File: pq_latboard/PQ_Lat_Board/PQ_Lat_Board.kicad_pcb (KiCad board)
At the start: 6 copper layers, 48 x 48 mm, 12 parts, among them IC1 TCN75AVUA713-VAO, J1 Conn_01x11_MountingPin

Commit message: designs updated
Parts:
- added REF**: MountingHole_2.2mm_M2_Pad, MountingHole:MountingHole_2.2mm_M2_Pad, F.Cu at (81.0, 46.0)
- added REF**: MountingHole_2.2mm_M2_Pad, MountingHole:MountingHole_2.2mm_M2_Pad, F.Cu at (121.0, 87.0)
- added REF**: MountingHole_2.2mm_M2_Pad, MountingHole:MountingHole_2.2mm_M2_Pad, F.Cu at (79.0, 84.0)
- added REF**: MountingHole_2.2mm_M2_Pad, MountingHole:MountingHole_2.2mm_M2_Pad, F.Cu at (119.0, 46.0)
- moved GA0 1.96 mm to (107.2, 55.6)
- moved GA1 1.96 mm to (109.6, 55.6)
- moved GA2 1.96 mm to (112.0, 55.6)
- moved IC1 1.96 mm to (103.6, 53.4)
- moved VA1 1.96 mm to (109.7, 50.3)
- moved VA2 1.96 mm to (112.0, 50.3)
- moved J1 1.96 mm to (107.7, 63.1)
- moved VA0 1.96 mm to (107.3, 50.3)
- moved JP1 1.96 mm to (82.8, 66.0)
- moved D7 1.96 mm to (99.0, 46.1)
- moved R1 1.96 mm to (98.1, 52.9)
- moved R2 1.96 mm to (100.5, 52.9)
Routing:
- net /GND: track 53.6 -> 41.4 mm, vias 68 -> 42

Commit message: lots of changes
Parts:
- removed D7: D_Photo, NSL_misc:SLCD-61N8
- removed R1, R2: 5k, easyeda:R0805
- added ?: , , F.Cu at (78.0, 66.0)
- added C1: 100 nF, Capacitor_SMD:C_0603_1608Metric, F.Cu at (100.1, 51.5)
- added D1: D_Photo, GGS_Miscellaneous:SLCD-61N8, B.Cu at (99.0, 45.5)
- GA0, GA1, GA2, VA0, VA1, VA2: value 5k -> 0R; footprint easyeda:R0805 -> Resistor_SMD:R_0805_2012Metric
- H1, H2, H3, H4: renamed from REF**; value MountingHole_2.2mm_M2_Pad -> MountingHole_Pad
- IC1: footprint easyeda:SOP65P490X110-8N -> Package_SO:SOP-8_3.9x4.9mm_P1.27mm
- moved GA0 0.20 mm to (107.4, 55.6)
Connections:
- net /GND renamed GND
- net /Pout renamed /SOLAR
- J1 pad 2: /ADCS_GND -> /ADCS
- J1 pad 3: /ADCS -> /VCC_MAG
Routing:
- net GND: track 41.4 -> 23.1 mm, vias 42 -> 34
- net /SDA: track 13.6 -> 8.59 mm
- net Net-(GA1-Pad2): track 17.0 -> 21.6 mm
- net /VCC: track 32.9 -> 29.1 mm
- net /SCL: track 12.2 -> 8.56 mm
- net /Antenna Connector: track 0.91 -> 3.73 mm
- net Net-(GA2-Pad2): track 12.6 -> 11.5 mm
- net (no net): vias 1 -> 0
- added copper zone on F.Cu, net /Antenna Connector
- added copper zone on B.Cu, net /SOLAR

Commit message: files changed
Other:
- board text added: "Extend temp sensor footprint fopr dual compatibility Hole positioning Solar Cells pads"
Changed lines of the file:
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@@
   (gr_line (start 120 62) (end 120 70) (layer "Edge.Cuts") (width 0.15))
   (gr_line (start 120 70) (end 123 70) (layer "Edge.Cuts") (width 0.15))
+  (gr_text "Extend temp sensor footprint fopr dual compatibility\nHole positioning\nSolar Cells pads" (at 93 111.4) (layer "F.Cu")
+    (effects (font (size 1.5 1.5) (thickness 0.3)) (justify left))
+  )
   (gr_text "LATERAL BOARD" (at 89.2 86.525) (layer "F.SilkS")
     (effects (font (size 2.032 2.032) (thickness 0.203)) (justify left))

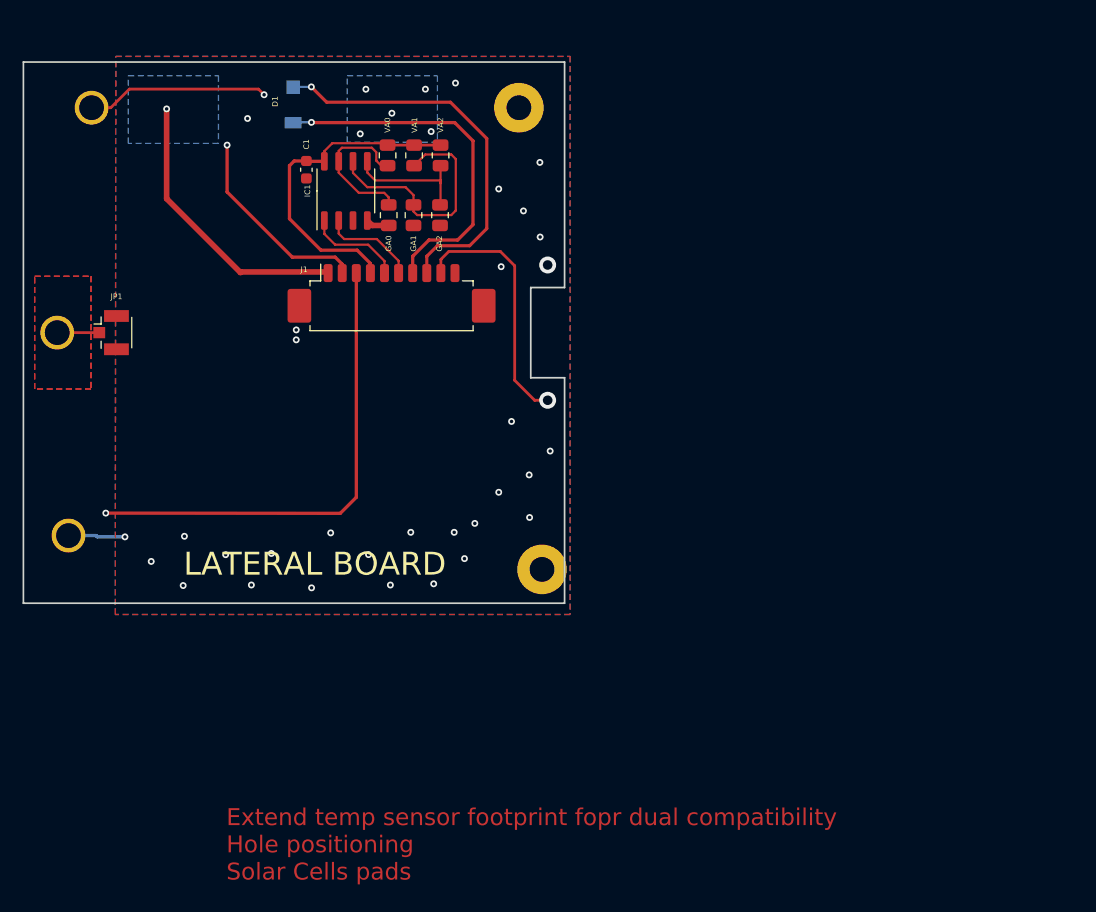
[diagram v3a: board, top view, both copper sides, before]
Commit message: Lateral, Bottom and MagY boards done
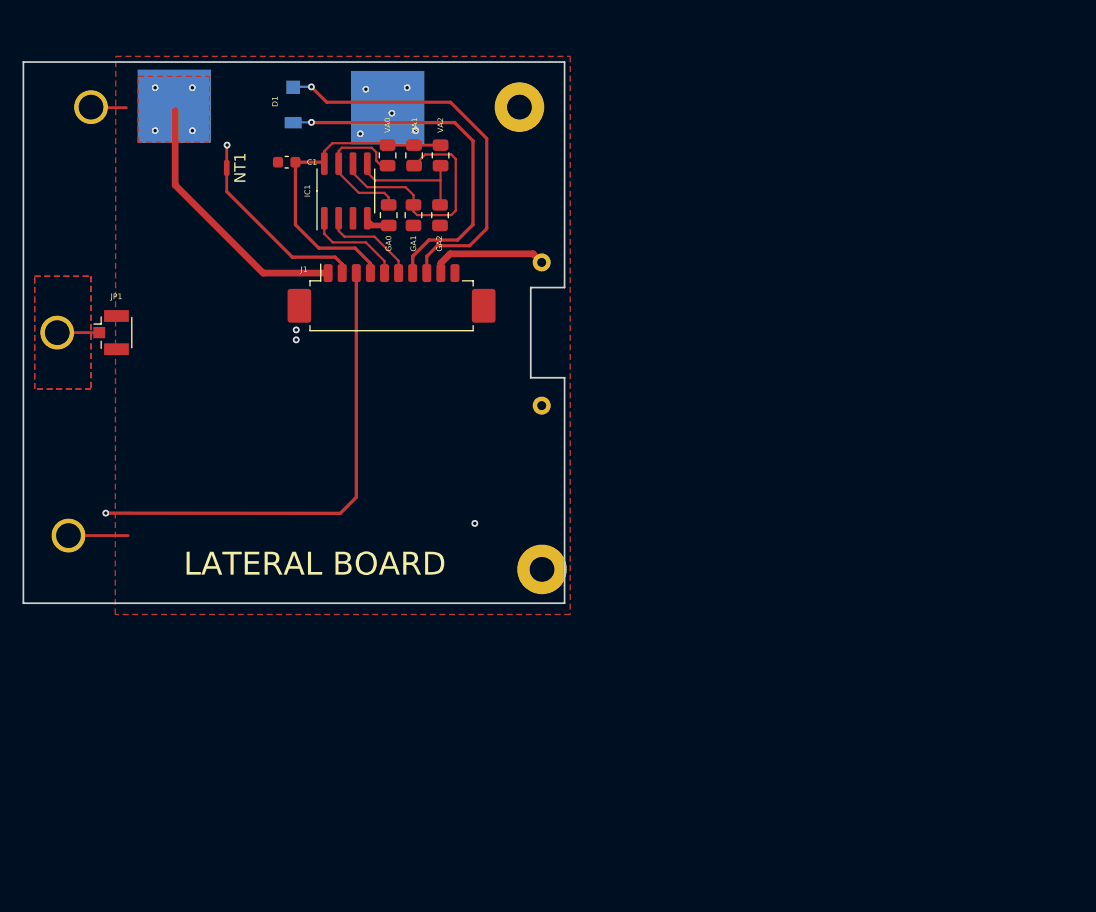
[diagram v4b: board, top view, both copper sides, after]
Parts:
- added NT1: NetTie_2, NetTie:NetTie-2_SMD_Pad0.5mm, F.Cu at (93.0, 51.4)
- added S1: SolarCell, NSL_power:Solar_Cell, B.Cu at (101.4, 68.9)
- added THT1: R, Resistor_THT:R_Axial_DIN0309_L9.0mm_D3.2mm_P12.70mm_Horizontal, B.Cu at (121.0, 59.8)
- C1: value 100 nF -> 1 uF
- IC1: value TCN75AVUA713-VAO -> TCN75AVOA713
- moved C1 1.87 mm to (98.4, 50.9), turned to 180 degrees
- moved H2 0.07 mm to (119.0, 46.0)
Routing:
- net /ADCS: track 9706.9 -> 15.2 mm, vias 5 -> 0
- net /VCC_MAG: track 0.00 -> 9690.4 mm, vias 0 -> 5
- net GND: track 23.1 -> 10.3 mm, vias 34 -> 5
- net /BURNCOMMS: track 22.1 -> 10.5 mm, vias 1 -> 0
- net /SOLAR: track 25.0 -> 23.4 mm, vias 1 -> 4
- net /VCC: track 29.1 -> 28.3 mm
- added copper zone on F.Cu, net /SOLAR
- removed copper zone on B.Cu, net /SOLAR
- removed copper zone on B.Cu, net GND
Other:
- board text added: "+Y"
- board text added: "-Y"
- board text removed: "Extend temp sensor footprint fopr dual compatibility Hole positioning Solar Cells pads"

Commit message: Merge branch 'main' of github.com:nanosatlab/pocat-hw
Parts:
- moved S1 1.02 mm to (100.4, 68.9)
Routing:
- net GND: track 10.3 -> 1.88 mm
- net /VCC_MAG: track 9690.4 -> 9695.5 mm
- net /SOLAR: track 23.4 -> 22.4 mm
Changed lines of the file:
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@@
       (effects (font (size 1 1) (thickness 0.15)))
     )
-    (fp_text user "gge22431" (at 0 0) (layer "Cmts.User")
+    (fp_text user "gge22431" (at 0 0) (layer "Cmts.User") hide
       (effects (font (size 1 1) (thickness 0.15)))
     )
@@
       (effects (font (size 1 1) (thickness 0.15)))
     )
-    (fp_text user "gge2a49f2e03dfde251" (at 0 0 90) (layer "Cmts.User")
+    (fp_text user "gge2a49f2e03dfde251" (at 0 0 90) (layer "Cmts.User") hide
       (effects (font (size 1 1) (thickness 0.15)))
     )
@@
     (property "Sheetfile" "PQ_Lat_Board.kicad_sch")
     (property "Sheetname" "")
+    (zone_connect 2)
     (attr exclude_from_pos_files)
     (fp_text reference "H1" (at 0 -3.2) (layer "F.SilkS") hide
@@
     (fp_circle (center 0 0) (end 2.2 0) (layer "Cmts.User") (width 0.15) (fill none))
     (fp_circle (center 0 0) (end 2.45 0) (layer "F.CrtYd") (width 0.05) (fill none))
-    (pad "1" thru_hole circle (at -0.05 -0.05) (size 3 3) (drill 2.2) (layers *.Cu *.Mask)
+    (pad "1" thru_hole circle (at -0.05 -0.05) (size 4.4 4.4) (drill 2.2) (layers *.Cu *.Mask)
       (net 12 "GND") (pinfunction "1") (pintype "input"))
   )
@@
     (property "Sheetfile" "PQ_Lat_Board.kicad_sch")
     (property "Sheetname" "")
+    (zone_connect 2)
     (attr exclude_from_pos_files)
     (fp_text reference "H4" (at 0 -3.2) (layer "F.SilkS") hide
@@
     (fp_circle (center 0 0) (end 2.2 0) (layer "Cmts.User") (width 0.15) (fill none))
     (fp_circle (center 0 0) (end 2.45 0) (layer "F.CrtYd") (width 0.05) (fill none))
-    (pad "1" thru_hole circle (at 0 0) (size 3 3) (drill 2.2) (layers *.Cu *.Mask)
+    (pad "1" thru_hole circle (at 0 0) (size 4.4 4.4) (drill 2.2) (layers *.Cu *.Mask)
       (net 12 "GND") (pinfunction "1") (pintype "input"))
   )
@@
   )
   (footprint "NSL_power:Solar_Cell" (layer "B.Cu")
-    (at 101.382 68.918 180)
+    (at 100.366 68.918 180)
     (property "Sheetfile" "PQ_Lat_Board.kicad_sch")
     (property "Sheetname" "")
@@
       (effects (font (size 1 1) (thickness 0.15)) (justify mirror))
     )
-    (fp_text user "gge14058" (at 1.6 -5.375 90) (layer "Cmts.User")
+    (fp_text user "gge14058" (at 1.6 -5.375 90) (layer "Cmts.User") hide
       (effects (font (size 1 1) (thickness 0.15)))
     )
@@
     (property "Sheetname" "")
     (attr through_hole)
-    (fp_text reference "THT1" (at 6.35 2.72 90) (layer "B.SilkS")
+    (fp_text reference "THT1" (at 6.256 1.854 90) (layer "B.SilkS")
       (effects (font (size 1 1) (thickness 0.15)) (justify mirror))
     )
@@
     (effects (font (size 2.032 2.032) (thickness 0.203)) (justify left))
   )
-  (gr_text "+Y\n" (at 97.2504 35.0852) (layer "Cmts.User")
+  (gr_text "+Y\n" (at 97.11 38.56) (layer "Cmts.User")
     (effects (font (size 5 5) (thickness 0.5)))
   )
-  (gr_text "-Y\n" (at 96.5392 97.7724) (layer "Cmts.User")
+  (gr_text "-Y\n" (at 96.61 93.56) (layer "Cmts.User")
     (effects (font (size 5 5) (thickness 0.5)))
+  )
+  (dimension (type aligned) (layer "B.SilkS")
+    (pts (xy 114.28 49.87) (xy 114.31 88.73))
+    (height 1.024501)
+    (gr_text "40 mm" (at 113.16 69.51 270.0442325) (layer "B.SilkS")
+      (effects (font (size 1 1) (thickness 0.15)) (justify mirror))
+    )
+    (format (units 3) (units_format 1) (precision 4) (override_value "40"))
+    (style (thickness 0.15) (arrow_length 1.27) (text_position_mode 2) (extension_height 0.58642) (extension_offset 0.5) keep_text_aligned)
+  )
+  (dimension (type aligned) (layer "B.SilkS")
+    (pts (xy 82.82 85.75) (xy 117.65 85.78))
+    (height -0.43481)
+    (gr_text "36 mm" (at 100.809075 84.86481 359.9506496) (layer "B.SilkS")
+      (effects (font (size 1 1) (thickness 0.15)) (justify mirror))
+    )
+    (format (units 3) (units_format 1) (precision 4) (override_value "36"))
+    (style (thickness 0.15) (arrow_length 1.27) (text_position_mode 2) (extension_height 0.58642) (extension_offset 0.5) keep_text_aligned)
   )
   (segment (start 103.25 49.6) (end 102.965 49.885) (width 0.2) (layer "F.Cu") (net 1))
@@
   (segment (start 78.000008 66.000008) (end 78 66) (width 0.25) (layer "F.Cu") (net 11))
   (segment (start 81.730007 66.000008) (end 78.000008 66.000008) (width 0.25) (layer "F.Cu") (net 11))
-  (segment (start 81.05 46.05) (end 84.136 46.05) (width 0.25) (layer "F.Cu") (net 12))
   (segment (start 105.9435 56.4955) (end 105.505 56.057) (width 0.5) (layer "F.Cu") (net 12))
   (segment (start 107.201 56.4955) (end 105.9435 56.4955) (width 0.5) (layer "F.Cu") (net 12))
-  (segment (start 84.302 84) (end 79 84) (width 0.25) (layer "F.Cu") (net 12))
-  (via (at 107.684 46.54) (size 0.61) (drill 0.305) (layers "F.Cu" "B.Cu") (net 12))
-  (via (at 109.798 48.09) (size 0.61) (drill 0.305) (layers "F.Cu" "B.Cu") (net 12))
-  (via (at 109.036 44.28) (size 0.61) (drill 0.305) (layers "F.Cu" "B.Cu") (net 12))
-  (via (at 104.876 48.368) (size 0.61) (drill 0.305) (layers "F.Cu" "B.Cu") (net 12))
-  (via (at 105.376 44.412) (size 0.61) (drill 0.305) (layers "F.Cu" "B.Cu") (net 12))
-  (segment (start 96.264784 60.718784) (end 88.462 52.916) (width 0.6) (layer "F.Cu") (net 13))
-  (segment (start 88.462 52.916) (end 88.462 46.312) (width 0.6) (layer "F.Cu") (net 13))
+  (via (at 106.242 46.54) (size 0.61) (drill 0.305) (layers "F.Cu" "B.Cu") (net 12))
+  (via (at 108.528 48.344) (size 0.61) (drill 0.305) (layers "F.Cu" "B.Cu") (net 12))
+  (via (at 108.528 44.026) (size 0.61) (drill 0.305) (layers "F.Cu" "B.Cu") (net 12))
+  (via (at 103.956 48.344) (size 0.61) (drill 0.305) (layers "F.Cu" "B.Cu") (net 12))
+  (via (at 103.956 44.026) (size 0.61) (drill 0.305) (layers "F.Cu" "B.Cu") (net 12))
   (segment (start 102.028617 60.718784) (end 96.264784 60.718784) (width 0.6) (layer "F.Cu") (net 13))
-  (via (at 86.684 48.09) (size 0.61) (drill 0.305) (layers "F.Cu" "B.Cu") (net 13))
-  (via (at 89.986 48.09) (size 0.61) (drill 0.305) (layers "F.Cu" "B.Cu") (net 13))
-  (via (at 89.986 44.28) (size 0.61) (drill 0.305) (layers "F.Cu" "B.Cu") (net 13))
-  (via (at 86.684 44.28) (size 0.61) (drill 0.305) (layers "F.Cu" "B.Cu") (net 13))
+  (segment (start 96.264784 60.718784) (end 87.7 52.154) (width 0.6) (layer "F.Cu") (net 13))
+  (segment (start 87.7 52.154) (end 87.7 47.582) (width 0.6) (layer "F.Cu") (net 13))
+  (via (at 85.922 48.09) (size 0.61) (drill 0.305) (layers "F.Cu" "B.Cu") (net 13))
+  (via (at 89.478 48.09) (size 0.61) (drill 0.305) (layers "F.Cu" "B.Cu") (net 13))
+  (via (at 89.478 44.026) (size 0.61) (drill 0.305) (layers "F.Cu" "B.Cu") (net 13))
+  (via (at 85.922 44.026) (size 0.61) (drill 0.305) (layers "F.Cu" "B.Cu") (net 13))
   (segment (start 93.034 49.402) (end 93.068 49.368) (width 0.25) (layer "F.Cu") (net 14))
-  (segment (start 103.108 82.028) (end 82.31 82.01) (width 0.293) (layer "F.Cu") (net 14))
   (segment (start 93.034 50.892) (end 93.034 49.402) (width 0.25) (layer "F.Cu") (net 14))
-  (segment (start 104.53 60.618) (end 104.53 80.605) (width 0.293) (layer "F.Cu") (net 14))
-  (segment (start 104.53 80.605) (end 103.108 82.028) (width 0.293) (layer "F.Cu") (net 14))
-  (via (at 82.31 82.01) (size 0.61) (drill 0.305) (layers "F.Cu" "B.Cu") (net 14))
+  (segment (start 81.76 82.028) (end 103.108 82.028) (width 0.293) (layer "F.Cu") (net 14))
+  (segment (start 104.53 80.605) (end 104.53 60.618) (width 0.293) (layer "F.Cu") (net 14))
+  (segment (start 80.334 80.602) (end 81.76 82.028) (width 0.293) (layer "F.Cu") (net 14))
+  (segment (start 103.108 82.028) (end 104.53 80.605) (width 0.293) (layer "F.Cu") (net 14))
+  (via (at 80.334 80.602) (size 0.61) (drill 0.305) (layers "F.Cu" "B.Cu") (net 14))
   (via (at 99.2 66.64) (size 0.61) (drill 0.305) (layers "F.Cu" "B.Cu") (net 14))
   (via (at 93.068 49.368) (size 0.61) (drill 0.305) (layers "F.Cu" "B.Cu") (net 14))
@@
   (segment (start 114.159 50.788) (end 83.788 50.788) (width 0.22) (layer "In1.Cu") (net 14))
   (segment (start 95.241 70.16) (end 103.161 70.16) (width 0.22) (layer "In1.Cu") (net 14))
+  (segment (start 80.334 80.602) (end 81.751 82.019) (width 0.2) (layer "In1.Cu") (net 14))
   (segment (start 90.849 74.56) (end 107.56 74.56) (width 0.22) (layer "In1.Cu") (net 14))
   (segment (start 107.999 74.994) (end 107.999 56.96) (width 0.22) (layer "In1.Cu") (net 14))
@@
   (segment (start 96.559 68.839) (end 97.134 68.839) (width 0.22) (layer "In1.Cu") (net 14))
   (segment (start 114.601 81.598) (end 114.601 50.356) (width 0.22) (layer "In1.Cu") (net 14))
+  (segment (start 81.751 82.019) (end 82.31 82.019) (width 0.2) (layer "In1.Cu") (net 14))
   (segment (start 111.08 78.067) (end 111.08 53.879) (width 0.22) (layer "In1.Cu") (net 14))
   (segment (start 89.96 75.451) (end 108.439 75.451) (width 0.22) (layer "In1.Cu") (net 14))
@@
     )
   )
+  (zone (net 12) (net_name "GND") (layer "F.Cu") (hatch edge 0.508)
+    (connect_pads (clearance 0.4))
+    (min_thickness 0.254) (filled_areas_thickness no)
+    (fill yes (thermal_gap 0.508) (thermal_bridge_width 0.508) (smoothing fillet) (radius 0.5))
+    (polygon
+      (pts
+        (xy 83.26 87.558361)
+        (xy 80.27 85.78)
+        (xy 80.29 82.26)
+        (xy 83.26 80.700361)
+      )
+    )
+  )
   (zone (net 13) (net_name "/SOLAR") (layer "F.Cu") (hatch edge 0.508)
     (priority 1)
@@
     (polygon
       (pts
-        (xy 91.51 49.106)
-        (xy 85.16 49.106)
-        (xy 85.16 43.264)
-        (xy 91.51 43.264)
+        (xy 91.256 49.106)
+        (xy 84.906 49.106)
+        (xy 84.906 43.264)
+        (xy 91.256 43.264)
       )
     )
+  )
+  (zone (net 12) (net_name "GND") (layer "F.Cu") (hatch edge 0.508)
+    (connect_pads (clearance 0.4))
+    (min_thickness 0.254) (filled_areas_thickness no)
+    (fill yes (thermal_gap 0.508) (thermal_bridge_width 0.508) (smoothing fillet) (radius 0.5))
+    (polygon
+      (pts
+        (xy 83.42 49.448)
+        (xy 80.43 47.669639)
+        (xy 80.45 44.149639)
+        (xy 83.42 42.59)
+      )
+    )

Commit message: Functional revision and finishing touches part I
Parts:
- removed ?: , 
- removed JP1: U.FL-R-SMT-1(10), Connector_Coaxial:U.FL_Hirose_U.FL-R-SMT-1_Vertical
- removed S1: SolarCell, NSL_power:Solar_Cell
- added H5: MountingHole_Pad, MountingHole:MountingHole_2.2mm_M2_DIN965_Pad_TopOnly, F.Cu at (78.5, 66.0)
- added J2: connector-coax, connector-nsl:C.FL-R-SMT-1(90), F.Cu at (83.9, 66.0)
- added SC1: Solar_Cell, power-nsl:Azur-Space-PQ-cut-SC, B.Cu at (100.5, 69.3)
- D1: value D_Photo -> SLCD-61N8; footprint GGS_Miscellaneous:SLCD-61N8 -> passive-nsl:SLCD-61N8
- moved D1 1.38 mm to (97.7, 45.8), turned to 180 degrees
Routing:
- net /PH-: track 32.0 -> 39.6 mm
- net /Antenna Connector: track 3.73 -> 4.41 mm
